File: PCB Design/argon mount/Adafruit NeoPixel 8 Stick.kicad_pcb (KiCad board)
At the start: 2 copper layers, 34.6 x 65 mm, 2 parts, among them CN2 1X4SMT

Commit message: argon mount
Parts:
- added R1: R, Resistor_THT:R_Axial_DIN0207_L6.3mm_D2.5mm_P7.62mm_Horizontal, F.Cu at (143.5, 104.9)
- added U1: MIC5219-2.85YM5, Package_TO_SOT_SMD:SOT-23-5, F.Cu at (143.3, 99.6)
- added U2: VL6180, Adafruit VL6180:VL6180, F.Cu at (135.9, 99.8)
- moved MD1 7.37 mm to (140.2, 133.9)
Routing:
- net Net-(CN2-Pad6): track 96.5 -> 65.2 mm
- net Net-(CN2-Pad3): track 35.4 -> 53.8 mm
- net Net-(CN2-Pad5): track 75.7 -> 89.2 mm
- net Net-(R1-Pad1): track 0.00 -> 13.4 mm
- net +5V: track 27.5 -> 37.2 mm
- net Net-(R1-Pad2): track 0.00 -> 5.64 mm
- net GND: track 0.00 -> 3.72 mm
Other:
- board size 34.6 x 65 mm -> 34.6 x 71.1 mm

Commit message: edited boards
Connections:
- MD1 pad 3.3V: +5V -> unconnected-(MD1-Pad3.3V)
- MD1 pad VBUS: unconnected-(MD1-PadVBUS) -> +5V
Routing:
- net +5V: track 37.2 -> 41.9 mm
- net Net-(CN2-Pad5): track 89.2 -> 88.6 mm
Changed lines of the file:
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@@
   (net 28 "unconnected-(MD1-PadNC)")
   (net 29 "unconnected-(MD1-PadRESET)")
-  (net 30 "unconnected-(MD1-PadVBUS)")
+  (net 30 "unconnected-(MD1-Pad3.3V)")
   (net 31 "unconnected-(U1-Pad4)")
   (net 32 "Net-(R1-Pad1)")
@@
       (net 7 "unconnected-(MD1-Pad3)") (pinfunction "P1.02/SCL1/UART1_CTS/SPI1_MOSI/PWM3") (pintype "bidirectional"))
     (pad "3.3V" thru_hole circle (at -10.16 -16.51) (size 1.57 1.57) (drill 1.02) (layers *.Cu)
-      (net 1 "+5V") (pinfunction "3.3V") (pintype "power_in"))
+      (net 30 "unconnected-(MD1-Pad3.3V)") (pinfunction "3.3V") (pintype "power_in"))
     (pad "4" thru_hole circle (at 10.16 8.89) (size 1.57 1.57) (drill 1.02) (layers *.Cu)
       (net 8 "unconnected-(MD1-Pad4)") (pinfunction "P1.08/SPI1_MISO/PWM1") (pintype "bidirectional"))
@@
       (net 29 "unconnected-(MD1-PadRESET)") (pinfunction "P0.18/~{RESET}") (pintype "bidirectional"))
     (pad "VBUS" thru_hole circle (at 10.16 -3.81) (size 1.57 1.57) (drill 1.02) (layers *.Cu)
-      (net 30 "unconnected-(MD1-PadVBUS)") (pinfunction "VBUS") (pintype "power_in"))
+      (net 1 "+5V") (pinfunction "VBUS") (pintype "power_in"))
     (model "eec.models/Particle_-_Argon.step"
       (offset (xyz -290.289763 645.1396703 67.24827699))
@@
   (gr_line (start 157.054 97.282) (end 157.054 161.036) (layer "Edge.Cuts") (width 0.05))
   (gr_line (start 122.428 97.536) (end 129.2 89.915998) (layer "Edge.Cuts") (width 0.05))
-  (segment (start 144.272 107.696) (end 146.685 105.283) (width 0.25) (layer "F.Cu") (net 1))
-  (segment (start 142.306 98.041723) (end 142.306 98.4305) (width 0.25) (layer "F.Cu") (net 1))
-  (segment (start 146.685 100.9095) (end 144.206 98.4305) (width 0.25) (layer "F.Cu") (net 1))
   (segment (start 143.573277 97.409) (end 142.938723 97.409) (width 0.25) (layer "F.Cu") (net 1))
-  (segment (start 142.311516 107.696) (end 144.272 107.696) (width 0.25) (layer "F.Cu") (net 1))
-  (segment (start 132.659516 117.348) (end 142.311516 107.696) (width 0.25) (layer "F.Cu") (net 1))
-  (segment (start 144.272 98.3645) (end 144.206 98.4305) (width 0.25) (layer "F.Cu") (net 1))
+  (segment (start 150.368 130.048) (end 151.4812 128.9348) (width 0.25) (layer "F.Cu") (net 1))
   (segment (start 144.272 93.98) (end 144.272 98.3645) (width 0.25) (layer "F.Cu") (net 1))
+  (segment (start 151.4812 105.7057) (end 144.206 98.4305) (width 0.25) (layer "F.Cu") (net 1))
   (segment (start 142.938723 97.409) (end 142.306 98.041723) (width 0.25) (layer "F.Cu") (net 1))
-  (segment (start 144.206 98.4305) (end 144.206 98.041723) (width 0.25) (layer "F.Cu") (net 1))
   (segment (start 144.206 98.041723) (end 143.573277 97.409) (width 0.25) (layer "F.Cu") (net 1))
-  (segment (start 146.685 105.283) (end 146.685 100.9095) (width 0.25) (layer "F.Cu") (net 1))
-  (segment (start 130.048 117.348) (end 132.659516 117.348) (width 0.25) (layer "F.Cu") (net 1))
+  (segment (start 151.4812 128.9348) (end 151.4812 105.7057) (width 0.25) (layer "F.Cu") (net 1))
   (via (at 144.272 93.98) (size 0.8) (drill 0.4) (layers "F.Cu" "B.Cu") (net 1))
   (segment (start 136.2618 100.1188) (end 136.2618 98.1802) (width 0.25) (layer "F.Cu") (net 2))
@@
   (segment (start 150.368 152.908) (end 148.255235 152.908) (width 0.25) (layer "B.Cu") (net 4))
   (segment (start 129.032 101.346) (end 129.032 92.329) (width 0.25) (layer "B.Cu") (net 4))
-  (segment (start 135.128 93.091) (end 135.128 93.726) (width 0.25) (layer "B.Cu") (net 4))
   (segment (start 130.556 90.805) (end 132.842 90.805) (width 0.25) (layer "B.Cu") (net 4))
   (segment (start 148.255235 152.908) (end 135.509 140.161765) (width 0.25) (layer "B.Cu") (net 4))
@@
   (segment (start 132.842 90.805) (end 135.128 93.091) (width 0.25) (layer "B.Cu") (net 4))
   (segment (start 133.731 100.965) (end 134.672 100.965) (width 0.25) (layer "F.Cu") (net 5))
-  (segment (start 134.672 100.965) (end 134.69 100.947) (width 0.25) (layer "F.Cu") (net 5))
   (via (at 133.731 100.965) (size 0.8) (drill 0.4) (layers "F.Cu" "B.Cu") (net 5))
   (segment (start 132.128 99.362) (end 133.731 100.965) (width 0.25) (layer "B.Cu") (net 5))

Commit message: clean up boards + generate some gerber files
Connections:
- net Net-(CN2-Pad5) renamed /SDA
- net Net-(CN2-Pad6) renamed /SCL
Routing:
- net /SCL: track 65.1 -> 66.3 mm

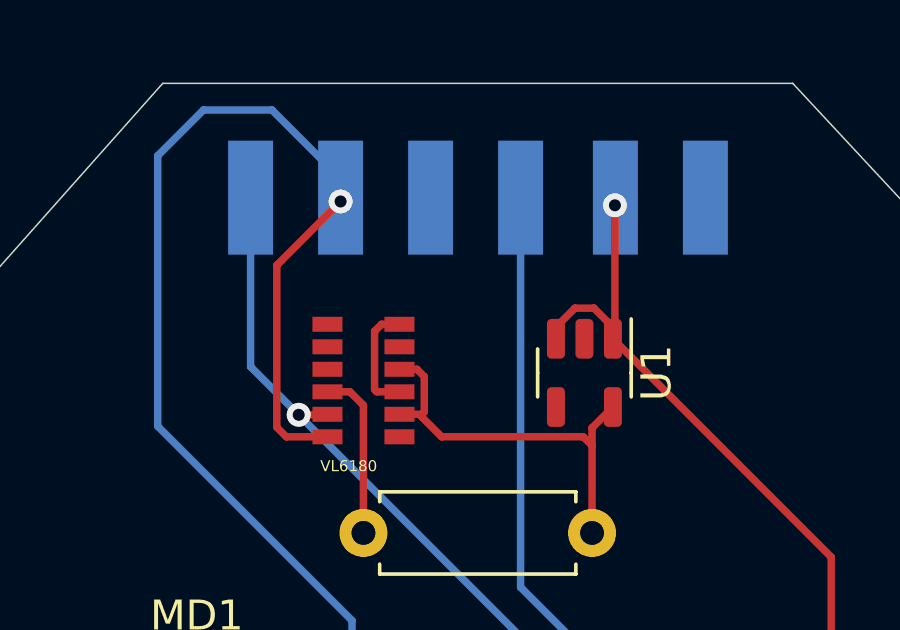
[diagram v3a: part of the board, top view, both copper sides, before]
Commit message: rm vias over pads
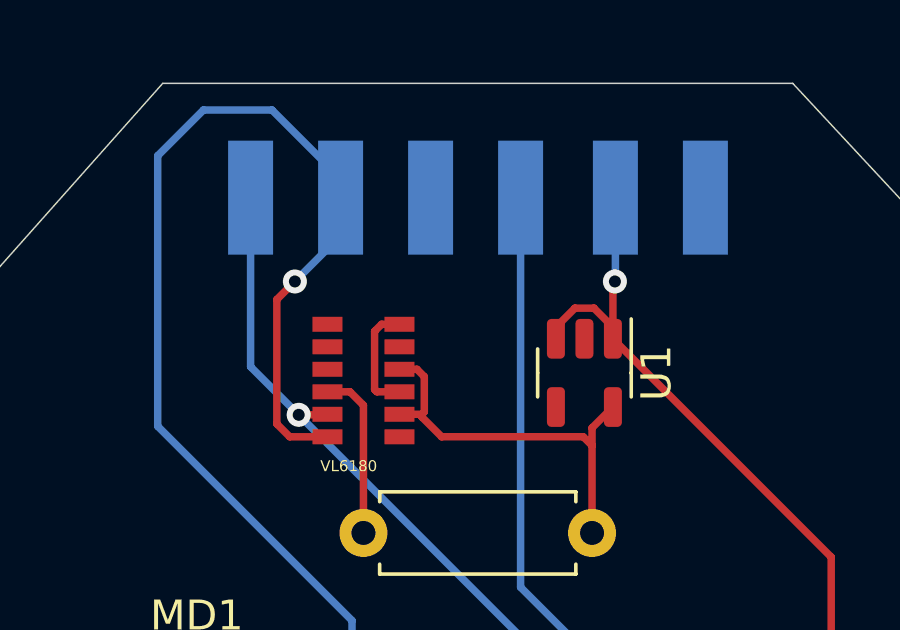
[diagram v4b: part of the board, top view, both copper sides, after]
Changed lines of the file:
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@@
   (gr_line (start 157.054 97.282) (end 157.054 161.036) (layer "Edge.Cuts") (width 0.05))
   (gr_line (start 122.428 97.536) (end 129.2 89.915998) (layer "Edge.Cuts") (width 0.05))
+  (segment (start 144.206 96.586) (end 144.272 96.52) (width 0.25) (layer "F.Cu") (net 1))
   (segment (start 143.573277 97.409) (end 142.938723 97.409) (width 0.25) (layer "F.Cu") (net 1))
   (segment (start 150.368 130.048) (end 151.4812 128.9348) (width 0.25) (layer "F.Cu") (net 1))
-  (segment (start 144.272 93.98) (end 144.272 98.3645) (width 0.25) (layer "F.Cu") (net 1))
   (segment (start 151.4812 105.7057) (end 144.206 98.4305) (width 0.25) (layer "F.Cu") (net 1))
+  (segment (start 144.206 98.4305) (end 144.206 96.586) (width 0.25) (layer "F.Cu") (net 1))
   (segment (start 142.938723 97.409) (end 142.306 98.041723) (width 0.25) (layer "F.Cu") (net 1))
   (segment (start 144.206 98.041723) (end 143.573277 97.409) (width 0.25) (layer "F.Cu") (net 1))
   (segment (start 151.4812 128.9348) (end 151.4812 105.7057) (width 0.25) (layer "F.Cu") (net 1))
-  (via (at 144.272 93.98) (size 0.8) (drill 0.4) (layers "F.Cu" "B.Cu") (net 1))
+  (via (at 144.272 96.52) (size 0.8) (drill 0.4) (layers "F.Cu" "B.Cu") (net 1))
+  (segment (start 144.288 96.504) (end 144.288 93.726) (width 0.25) (layer "B.Cu") (net 1))
+  (segment (start 144.272 96.52) (end 144.288 96.504) (width 0.25) (layer "B.Cu") (net 1))
   (segment (start 136.2618 100.1188) (end 136.2618 98.1802) (width 0.25) (layer "F.Cu") (net 2))
   (segment (start 136.495 97.947) (end 137.09 97.947) (width 0.25) (layer "F.Cu") (net 2))
@@
   (segment (start 143.891 109.474) (end 143.891 132.588) (width 0.25) (layer "B.Cu") (net 3))
   (segment (start 141.128 93.726) (end 141.128 106.711) (width 0.25) (layer "B.Cu") (net 3))
-  (segment (start 135.128 93.853) (end 133.0028 95.9782) (width 0.25) (layer "F.Cu") (net 4))
-  (segment (start 133.32 101.697) (end 134.69 101.697) (width 0.25) (layer "F.Cu") (net 4))
-  (segment (start 133.0028 95.9782) (end 133.0028 101.3798) (width 0.25) (layer "F.Cu") (net 4))
-  (segment (start 133.0028 101.3798) (end 133.32 101.697) (width 0.25) (layer "F.Cu") (net 4))
-  (via (at 135.128 93.853) (size 0.8) (drill 0.4) (layers "F.Cu" "B.Cu") (net 4))
+  (segment (start 133.0028 97.1212) (end 133.604 96.52) (width 0.25) (layer "F.Cu") (net 4))
+  (segment (start 133.433169 101.697) (end 133.0028 101.266631) (width 0.25) (layer "F.Cu") (net 4))
+  (segment (start 133.0028 101.266631) (end 133.0028 97.1212) (width 0.25) (layer "F.Cu") (net 4))
+  (segment (start 134.69 101.697) (end 133.433169 101.697) (width 0.25) (layer "F.Cu") (net 4))
+  (via (at 133.604 96.52) (size 0.8) (drill 0.4) (layers "F.Cu" "B.Cu") (net 4))
   (segment (start 135.509 107.823) (end 129.032 101.346) (width 0.25) (layer "B.Cu") (net 4))
   (segment (start 150.368 152.908) (end 148.255235 152.908) (width 0.25) (layer "B.Cu") (net 4))
@@
   (segment (start 130.556 90.805) (end 132.842 90.805) (width 0.25) (layer "B.Cu") (net 4))
   (segment (start 148.255235 152.908) (end 135.509 140.161765) (width 0.25) (layer "B.Cu") (net 4))
+  (segment (start 135.128 94.996) (end 135.128 93.726) (width 0.25) (layer "B.Cu") (net 4))
   (segment (start 135.509 140.161765) (end 135.509 107.823) (width 0.25) (layer "B.Cu") (net 4))
   (segment (start 129.032 92.329) (end 130.556 90.805) (width 0.25) (layer "B.Cu") (net 4))
+  (segment (start 133.604 96.52) (end 135.128 94.996) (width 0.25) (layer "B.Cu") (net 4))
   (segment (start 132.842 90.805) (end 135.128 93.091) (width 0.25) (layer "B.Cu") (net 4))
   (segment (start 133.731 100.965) (end 134.672 100.965) (width 0.25) (layer "F.Cu") (net 5))
